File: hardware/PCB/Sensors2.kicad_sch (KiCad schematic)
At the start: 25 parts, among them J12 Micro SD Adapter, J13 Relays, J14 Screw_Terminal_01x03, J201 Micro_SD_Card_Det2, J202 Screw_Terminal_01x03, J6 Screw_Terminal_01x03, K1 SANYOU_SRD_Form_C, K2 SANYOU_SRD_Form_C, K201 SANYOU_SRD_Form_C, Q1 NPN, Q201 NPN, Q3 NPN, U2 PC817C, U202 PC817C, U5 PC817C

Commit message: PCB
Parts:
- added C2: 10u, Capacitor_SMD:C_1206_3216Metric, symbol Device:C
- added J_BAT1: Conn_01x02, TerminalBlock:TerminalBlock_MaiXu_MX126-5.0-02P_1x02_P5.00mm, symbol Connector_Generic:Conn_01x02
- added J_R: 100W 1R, TerminalBlock:TerminalBlock_MaiXu_MX126-5.0-02P_1x02_P5.00mm, symbol Connector_Generic:Conn_01x02
- added Q2: IRLZ44N, Package_TO_SOT_THT:TO-220-3_Vertical, symbol Transistor_FET:IRLZ44N
- added R5: 1k, Resistor_SMD:R_0805_2012Metric, symbol Device:R
- added U103: LM358, footprints:LM358, symbol Amplifier_Operational:LM358
- added U4: LM358, Package_SO:SOIC-8_3.9x4.9mm_P1.27mm, symbol Amplifier_Operational:LM358
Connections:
- net +3V3: now also U4.8 (V+)
- net GND: now also C2.2, J_BAT1.2 (Pin_2), J_R.2 (Pin_2), U4.4 (V-)
- new net active_load_Vin+: C2.1, R5.2, U4.3 (+)
- new net active_load_Vin-: J_R.1 (Pin_1), Q2.3 (S), U4.2 (-)
- new net active_load_Vout: Q2.1 (G), U4.1
- new net battery_load: J_BAT1.1 (Pin_1), Q2.2 (D)
- new net pwm_current_sel: R5.1
- no-connect marks 1 -> 4
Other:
- note added: "Bat+"
- note added: "Bat-"
- note added: "I=U_{PWM}/R"
- note added: "https://piotr-gorecki.pl/yk012-wspolnie-projektujemy-uniwersalne-obciazenie-aktywne/"

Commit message: pcb sensors
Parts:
- U2, U202, U5: footprint (none) -> Package_DIP:DIP-4_W7.62mm_LongPads
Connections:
- net K1_COM: now reaches J202.2 (Pin_2), K201.1
- net K1_DA: now reaches D201.2 (A), K201.2, Q201.1 (C)
- net K1_NO: now reaches J202.3 (Pin_3), K201.3
- net K1_NC: now reaches J202.1 (Pin_1), K201.4
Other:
- moved on the sheet: J202

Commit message: pcb sensors
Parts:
- removed D2, D201, D4: 1N4148, Diode_SMD:D_SOD-323, symbol Device:D
- removed J12: Micro SD Adapter, Connector_PinHeader_2.54mm:PinHeader_1x06_P2.54mm_Vertical, symbol Connector:Conn_01x06_Pin
- removed J13: Relays, Connector_PinHeader_2.54mm:PinHeader_1x06_P2.54mm_Vertical, symbol Connector:Conn_01x06_Pin
- removed J14, J202, J6: Screw_Terminal_01x03, symbol Connector:Screw_Terminal_01x03
- removed J201: Micro_SD_Card_Det2, symbol Connector:Micro_SD_Card_Det2
- removed JP202: SolderJumper_2_Open, Jumper:SolderJumper-2_P1.3mm_Open_TrianglePad1.0x1.5mm, symbol Jumper:SolderJumper_2_Open
- removed J_R: 100W 1R, TerminalBlock:TerminalBlock_MaiXu_MX126-5.0-02P_1x02_P5.00mm, symbol Connector_Generic:Conn_01x02
- removed K1, K2, K201: SANYOU_SRD_Form_C, Relay_THT:Relay_SPDT_SANYOU_SRD_Series_Form_C, symbol Relay:SANYOU_SRD_Form_C
- removed Q1, Q201, Q3: NPN, symbol Simulation_SPICE:NPN
- removed R1, R2, R201, R202, R7, R8: 220R, Resistor_SMD:R_0805_2012Metric, symbol Device:R
- removed U2, U202, U5: PC817C, Package_DIP:DIP-4_W7.62mm_LongPads, symbol Isolator:VO615A
- added C10, C11, C301: 100n, Capacitor_SMD:C_0805_2012Metric, symbol Device:C
- added C302: 1u, Capacitor_SMD:C_0805_2012Metric, symbol Device:C
- added J302: Micro_SD_Card, footprints:microSD, symbol Connector:Micro_SD_Card
- added J303: Micro SD, footprints:board_smd_sd, symbol Connector:Conn_01x08_Pin
- added J304: Conn_01x08_Socket, Connector_PinHeader_2.54mm:PinHeader_1x06_P2.54mm_Vertical, symbol Connector:Conn_01x08_Socket
- added J9: J_BMP3, Connector_PinHeader_2.54mm:PinHeader_1x06_P2.54mm_Vertical, symbol Connector:Conn_01x06_Pin
- added J_R1: 100W 1R, symbol Connector:Screw_Terminal_01x02
- added R301, R302, R303, R304, R305: 5.1k, Resistor_SMD:R_0805_2012Metric, symbol Device:R
- added U9: BME280, Package_LGA:Bosch_LGA-8_2.5x2.5mm_P0.65mm_ClockwisePinNumbering, symbol Sensor:BME280
- U4: footprint Package_SO:SOIC-8_3.9x4.9mm_P1.27mm -> footprints:LM358; JLCPCB Part C5423 -> C2977710; Link https://jlcpcb.com/partdetail/TexasInstruments-LM358DR/C5423 -> (none); MFR Part LM358DR -> (none); Manufacturer Texas Instruments -> (none)
- renumbered U103 to U4
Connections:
- net +3V3: now also C10.1, C11.1, C301.1, C302.1, J302.4 (VDD), J303.7 (Pin_7), J304.7 (Pin_7), J9.1 (Pin_1), R301.1, R302.1, R303.1, R304.1, R305.1, U9.6 (VDDIO), U9.8 (VDD); no longer U4.8 (V+)
- net GND: now also C10.2, C11.2, C301.2, C302.2, J302.6 (VSS), J303.6 (Pin_6), J304.6 (Pin_6), J9.2 (Pin_2), J_R1.2 (Pin_2), U9.1 (GND), U9.7 (GND)
- net SD_CS: now also J302.2 (DAT3/CD), J303.5 (Pin_5), J304.5 (Pin_5), R301.2
- net SPI_MISO: now also J302.7 (DAT0), J303.2 (Pin_2), J304.2 (Pin_2), J9.6 (Pin_6), R303.2, U9.5 (SDO)
- net SPI_MOSI: now also J302.3 (CMD), J303.4 (Pin_4), J304.4 (Pin_4), J9.4 (Pin_4), R302.2, U9.3 (SDI)
- net SPI_SCK: now also J302.5 (CLK), J303.3 (Pin_3), J304.3 (Pin_3), J9.3 (Pin_3), U9.4 (SCK)
- net active_load_Vin-: now also J_R1.1 (Pin_1)
- net battery_load renamed Bat_load+
- new net: J302.1 (DAT2), R304.2
- new net: J302.8 (DAT1), R305.2
- new net +5V: U4.8 (V+)
- new net BMP3_CS: J9.5 (Pin_5), U9.2 (CSB)
- no-connect marks 4 -> 8
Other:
- note added: "BME280"
- note added: "VCC GND SCK MOSI CS MISO"
- note added: "microSD"
- note removed: "CS_SD karta"
- note removed: "Przerwane w trakcie roboty dodać footprinty"
- note removed: "i THT na moduł i na smd"
- note removed: "jaks popularna obudowa karty micor sd połączneia z kartą na płytce i wyjscia na zewnętrzny moduł solder brige tylk na CS na plytce"

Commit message: Rough Layout pcb
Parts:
- removed C301: 100n, Capacitor_SMD:C_0805_2012Metric, symbol Device:C
- removed C302: 1u, Capacitor_SMD:C_0805_2012Metric, symbol Device:C
- removed J302: Micro_SD_Card, footprints:microSD, symbol Connector:Micro_SD_Card
- removed J303: Micro SD, footprints:board_smd_sd, symbol Connector:Conn_01x08_Pin
- removed J304: Conn_01x08_Socket, Connector_PinHeader_2.54mm:PinHeader_1x06_P2.54mm_Vertical, symbol Connector:Conn_01x08_Socket
- removed R301, R302, R303, R304, R305: 5.1k, Resistor_SMD:R_0805_2012Metric, symbol Device:R
- added TP301, TP302, TP303: TestPoint, TestPoint:TestPoint_Pad_D1.5mm, symbol Connector:TestPoint
- J301: renamed from J_BAT1; value Conn_01x02 -> BAT_LOAD; now left out of the parts list
- J302: renamed from J9; footprint Connector_PinHeader_2.54mm:PinHeader_1x06_P2.54mm_Vertical -> Connector_JST:JST_XH_B6B-XH-A_1x06_P2.50mm_Vertical; Link (none) -> https://pl.aliexpress.com/item/1005006960863510.html?spm=a2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; now left out of the parts list
- J303: renamed from J_R1; footprint (none) -> TerminalBlock_Phoenix:TerminalBlock_Phoenix_MKDS-1,5-2_1x02_P5.00mm_Horizontal; now left out of the parts list
- U301: renamed from U4; footprint footprints:LM358 -> Package_SO:SOIC-8_3.9x4.9mm_P1.27mm; JLCPCB Part C2977710 -> C7950; Link (none) -> https://jlcpcb.com/partdetail/onsemi-LM358DR2G/C7950; MFR Part (none) -> LM358DR2G; Manufacturer (none) -> onsemi
- renumbered C11 to C301, C10 to C302, C2 to C303, Q2 to Q301, R5 to R301, U9 to U302
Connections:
- net active_load_Vin+: now also TP301.1
- net active_load_Vin-: now also TP303.1
- net active_load_Vout: now also TP302.1
- no-connect marks 8 -> 3
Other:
- note removed: "microSD"
- moved on the sheet: C301, C302, J302, J303, Q301, U302

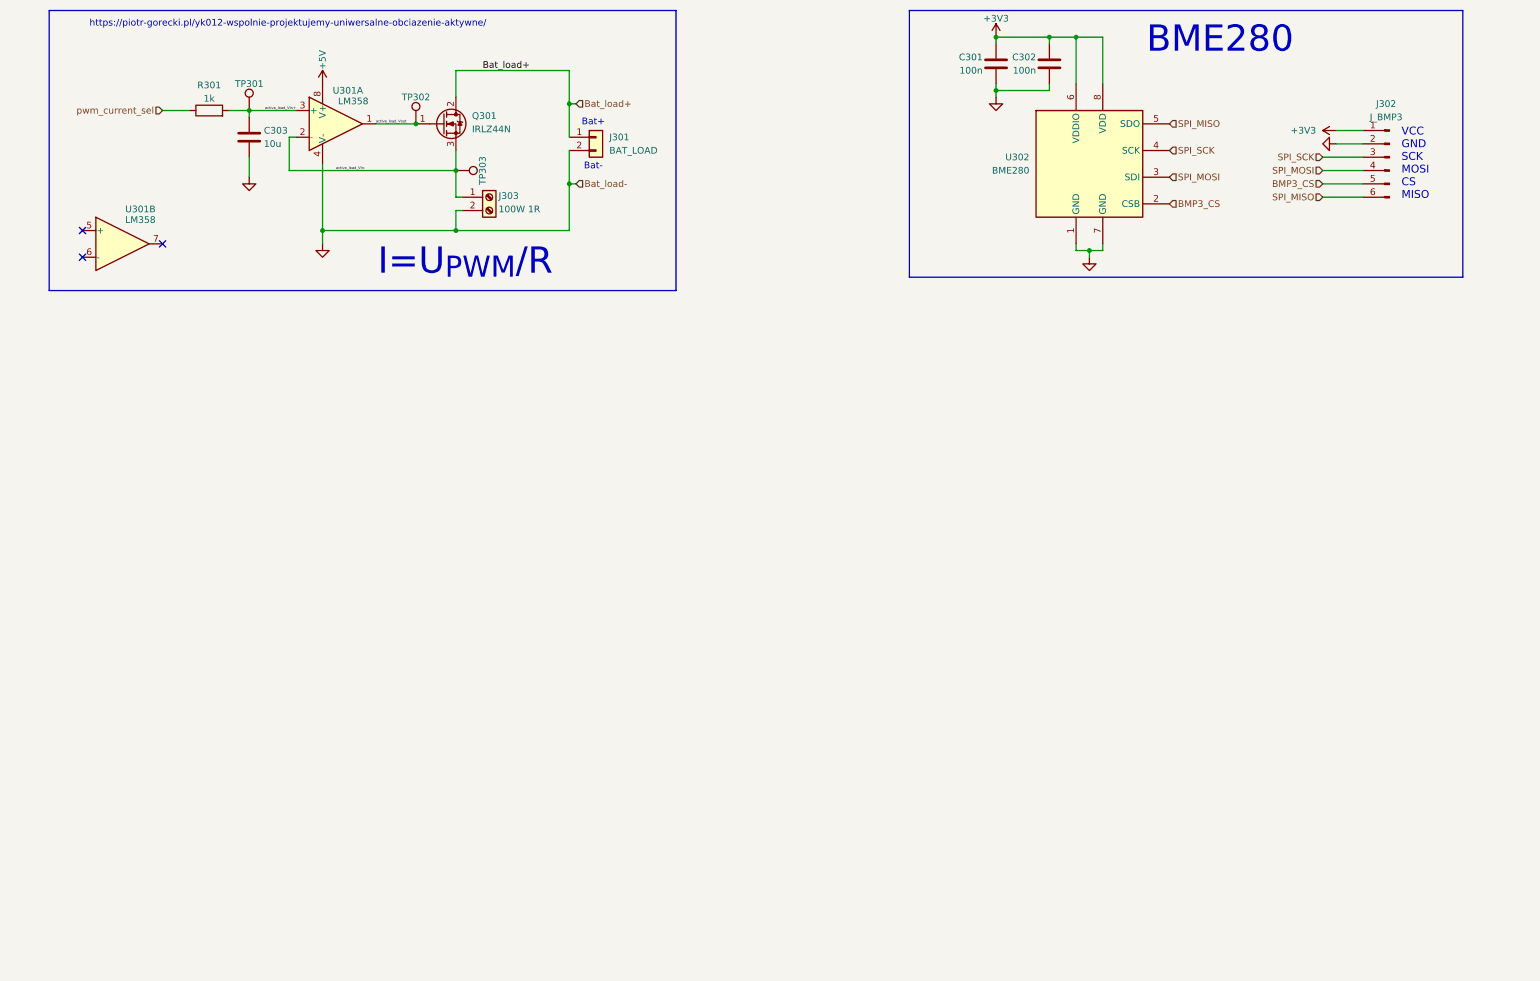
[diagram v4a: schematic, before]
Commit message: pcb XL4015
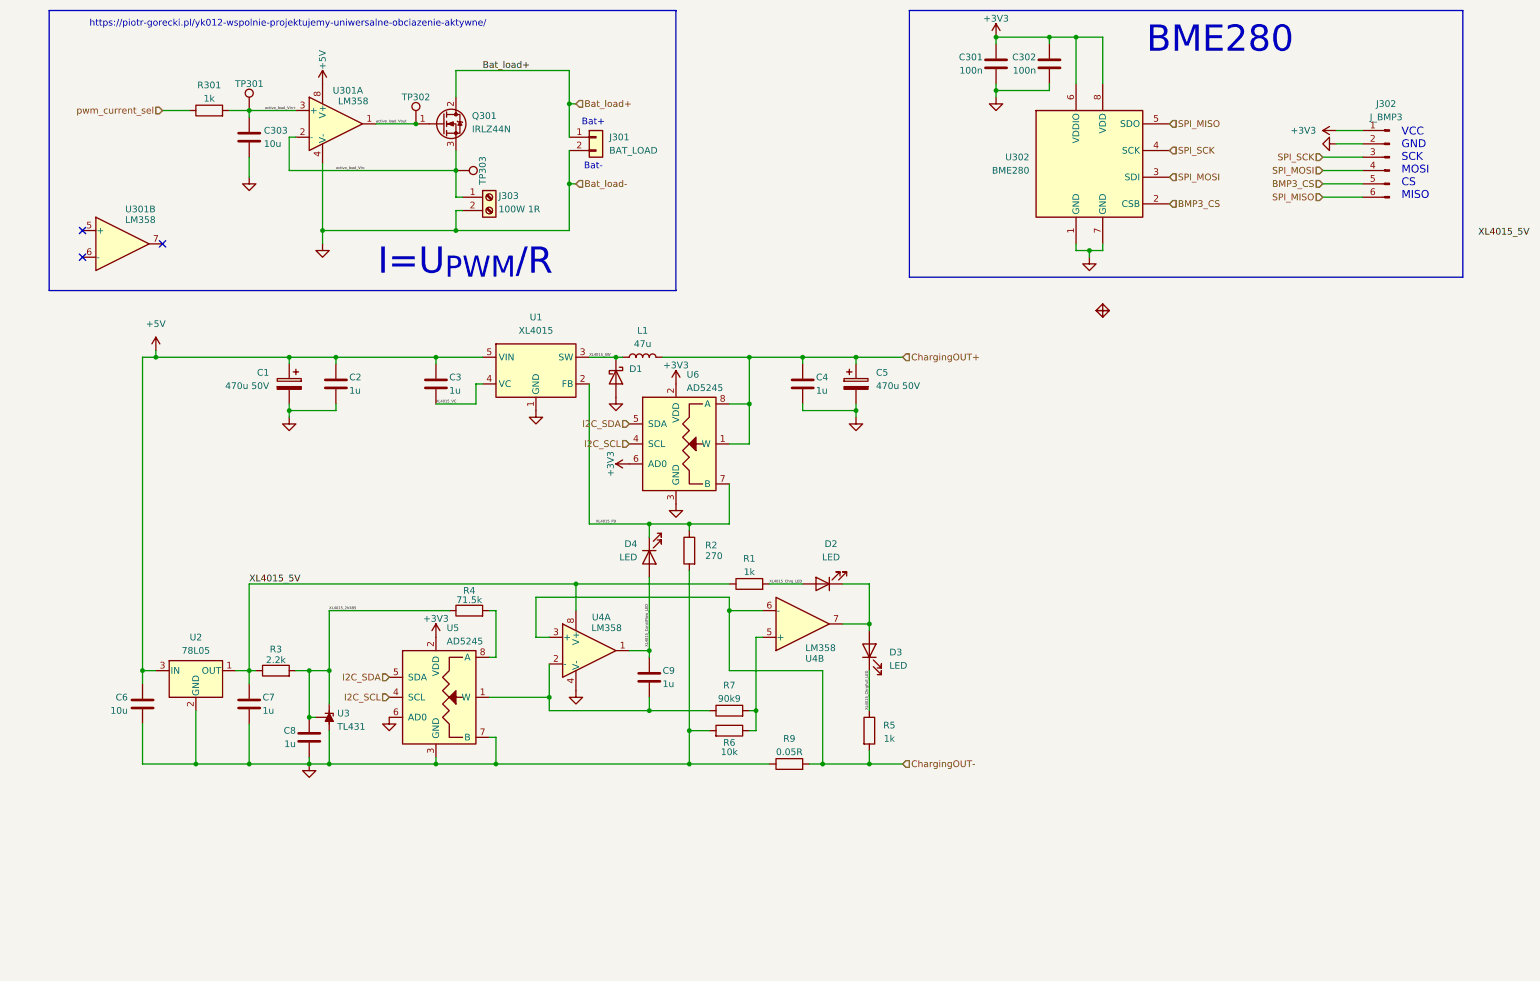
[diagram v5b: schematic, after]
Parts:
- added C1, C5: 470u 50V, Capacitor_SMD:C_Elec_10x10.2, symbol Device:C_Polarized
- added C2, C3, C4, C7, C8, C9: 1u, Capacitor_SMD:C_0805_2012Metric, symbol Device:C
- added C6: 10u, Capacitor_SMD:C_1206_3216Metric, symbol Device:C
- added D1: MBRD1045, Diode_SMD:D_SMA, symbol Device:D_Schottky
- added D2, D3, D4: LED, LED_SMD:LED_0805_2012Metric, symbol Device:LED
- added L1: 47u, Inductor_THT:L_Toroid_Vertical_L16.0mm_W8.0mm_P7.62mm, symbol Device:L
- added R1, R5: 1k, Resistor_SMD:R_0805_2012Metric, symbol Device:R
- added R2: 270, Resistor_SMD:R_0805_2012Metric, symbol Device:R
- added R3: 2.2k, Resistor_SMD:R_0805_2012Metric, symbol Device:R
- added R4: 71.5k, Resistor_SMD:R_0805_2012Metric, symbol Device:R
- added R6: 10k, Resistor_SMD:R_0805_2012Metric, symbol Device:R
- added R7: 90k9, Resistor_SMD:R_0805_2012Metric, symbol Device:R
- added R9: 0.05R, Resistor_SMD:R_2512_6332Metric, symbol Device:R
- added U1: XL4015, Package_TO_SOT_SMD:TO-263-5_TabPin3, symbol Regulator_Switching:XL4015
- added U2: 78L05, Package_TO_SOT_SMD:SOT-89-3, symbol Regulator_Linear:L78L05_SOT89
- added U3: TL431, Package_TO_SOT_SMD:SOT-23-3, symbol Reference_Voltage:TL431DBZ
- added U4: LM358, Package_SO:SOIC-8_3.9x4.9mm_P1.27mm, symbol Amplifier_Operational:LM358
- added U5, U6: AD5245, Package_TO_SOT_SMD:SOT-23-8, symbol footprints:AD5245
- U301: Manufacturer onsemi -> onsemi
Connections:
- net +3V3: now also U5.2 (VDD), U6.2 (VDD), U6.6 (AD0)
- net +5V: now also C1.1, C2.1, C3.1, C6.1, U1.5 (VIN), U2.3 (IN)
- net GND: now also C1.2, C2.2, C4.2, C5.2, C6.2, C7.2, C8.2, D1.2 (A), R2.2, R6.2, R9.1, U1.1 (GND), U2.2 (GND), U3.3 (A), U4.4 (V-), U5.3 (GND), U5.6 (AD0), U5.7 (B), U6.3 (GND)
- new net: C9.2, R7.1, U4.2 (-), U5.1 (W)
- new net: R4.2, U5.8 (A)
- new net: D2.1 (K), D3.2 (A), U4.7
- new net: R6.1, R7.2, U4.5 (+)
- new net ChargingOUT+: C4.1, C5.1, L1.2, U6.1 (W), U6.8 (A)
- new net ChargingOUT-: R5.2, R9.2, U4.3 (+), U4.6 (-)
- new net I2C_SCL: U5.4 (SCL), U6.4 (SCL)
- new net I2C_SDA: U5.5 (SDA), U6.5 (SDA)
- new net XL4015_2V495: C8.1, R3.2, R4.1, U3.1 (K), U3.2 (REF)
- new net XL4015_5V: C7.1, R1.1, R3.1, U2.1 (OUT), U4.8 (V+)
- new net XL4015_ChrgFull_LED: D3.1 (K), R5.1
- new net XL4015_Chrg_LED: D2.2 (A), R1.2
- new net XL4015_ConstFlow_LED: C9.1, D4.2 (A), U4.1
- new net XL4015_FB: D4.1 (K), R2.1, U1.2 (FB), U6.7 (B)
- new net XL4015_SW: D1.1 (K), L1.1, U1.3 (SW)
- new net XL4015_VC: C3.2, U1.4 (VC)

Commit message: XL4015 CC, relays
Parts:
- removed C1, C5: 470u 50V, Capacitor_SMD:C_Elec_10x10.2, symbol Device:C_Polarized
- removed C2, C3, C4, C7, C8, C9: 1u, Capacitor_SMD:C_0805_2012Metric, symbol Device:C
- removed C6: 10u, Capacitor_SMD:C_1206_3216Metric, symbol Device:C
- removed D1: MBRD1045, Diode_SMD:D_SMA, symbol Device:D_Schottky
- removed D2, D3, D4: LED, LED_SMD:LED_0805_2012Metric, symbol Device:LED
- removed L1: 47u, Inductor_THT:L_Toroid_Vertical_L16.0mm_W8.0mm_P7.62mm, symbol Device:L
- removed R1, R5: 1k, Resistor_SMD:R_0805_2012Metric, symbol Device:R
- removed R2: 270, Resistor_SMD:R_0805_2012Metric, symbol Device:R
- removed R3: 2.2k, Resistor_SMD:R_0805_2012Metric, symbol Device:R
- removed R4: 71.5k, Resistor_SMD:R_0805_2012Metric, symbol Device:R
- removed R6: 10k, Resistor_SMD:R_0805_2012Metric, symbol Device:R
- removed R7: 90k9, Resistor_SMD:R_0805_2012Metric, symbol Device:R
- removed R9: 0.05R, Resistor_SMD:R_2512_6332Metric, symbol Device:R
- removed U1: XL4015, Package_TO_SOT_SMD:TO-263-5_TabPin3, symbol Regulator_Switching:XL4015
- removed U2: 78L05, Package_TO_SOT_SMD:SOT-89-3, symbol Regulator_Linear:L78L05_SOT89
- removed U3: TL431, Package_TO_SOT_SMD:SOT-23-3, symbol Reference_Voltage:TL431DBZ
- removed U4: LM358, Package_SO:SOIC-8_3.9x4.9mm_P1.27mm, symbol Amplifier_Operational:LM358
- removed U5, U6: AD5245, Package_TO_SOT_SMD:SOT-23-8, symbol footprints:AD5245
- added H405, H406: ResistorMountingHole, MountingHole:MountingHole_3.2mm_M3_Pad, symbol Mechanical:MountingHole
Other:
- moved on the sheet: C301, C302, C303, J301, J302, J303, Q301, R301, TP301, TP302, TP303, U301A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
